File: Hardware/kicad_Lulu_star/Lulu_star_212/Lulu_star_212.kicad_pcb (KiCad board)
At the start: 2 copper layers, 16.7 x 14.9 mm, 8 parts, among them J1 Conn_01x03_Female, P1 Soldering_pad, Q1 Q_NMOS_GSD, T1 Q_NPN_BEC

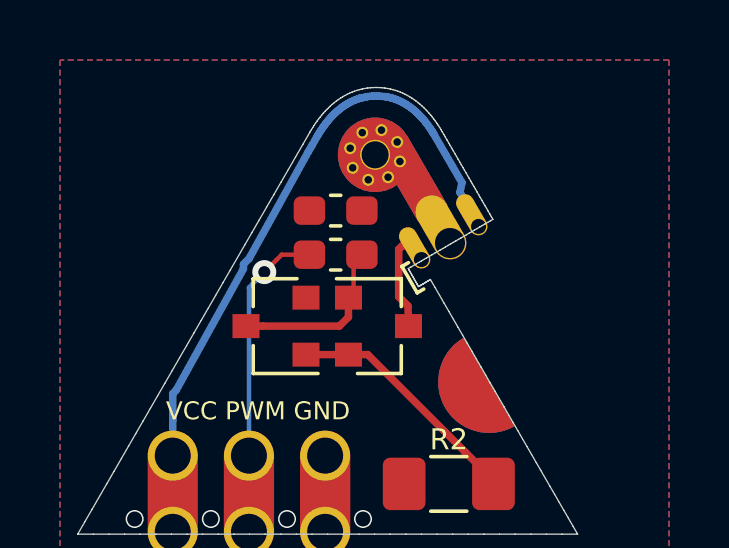
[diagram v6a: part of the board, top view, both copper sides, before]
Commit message: Correct the thermal pad GND connection
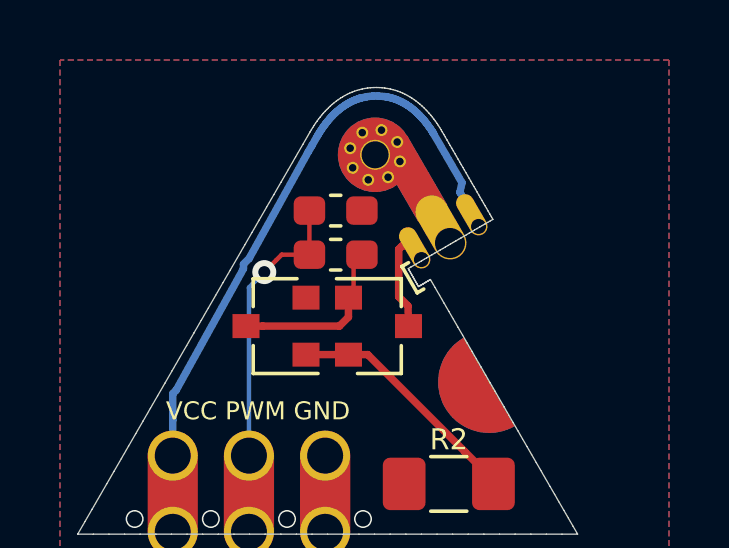
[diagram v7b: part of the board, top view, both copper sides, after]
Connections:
- LED1 pad : (no net) -> GND
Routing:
- net /PWM: track 7.80 -> 9.27 mm
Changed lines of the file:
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@@
     (thickness 1)
     (drawings 292)
-    (tracks 99)
+    (tracks 100)
     (zones 0)
     (modules 8)
@@
     (44 Edge.Cuts user)
     (45 Margin user)
-    (46 B.CrtYd user hide)
-    (47 F.CrtYd user hide)
-    (48 B.Fab user hide)
-    (49 F.Fab user hide)
+    (46 B.CrtYd user)
+    (47 F.CrtYd user)
+    (48 B.Fab user)
+    (49 F.Fab user)
   )
   (setup
@@
     (mod_text_size 1 1)
     (mod_text_width 0.15)
-    (pad_size 1.05 0.95)
+    (pad_size 2.48 2.48)
     (pad_drill 0)
     (pad_to_mask_clearance 0)
@@
     (add_net "Net-(Q1-Pad1)")
   )
-  (module Lulu_footprints:Lulu_side_LED locked (layer F.Cu)
+  (module Lulu_footprints:Lulu_side_LED (layer F.Cu)
     (at 74.64 35.4 30.1)
     (descr "LED Cree-XP http://www.cree.com/~/media/Files/Cree/LED-Components-and-Modules/XLamp/Data-and-Binning/XLampXPE2.pdf")
@@
       (effects (font (size 1 1) (thickness 0.15)))
     )
+    (fp_arc (start 0 0.6) (end -0.9 0.6) (angle -180) (layer F.Fab) (width 0.1))
+    (fp_line (start -1.778 -0.127) (end -1.524 -0.127) (layer F.SilkS) (width 0.12))
+    (fp_line (start -1.778 0.889) (end -1.778 -0.127) (layer F.SilkS) (width 0.12))
+    (fp_line (start -1.524 0.889) (end -1.778 0.889) (layer F.SilkS) (width 0.12))
+    (fp_line (start -1.523999 10.922) (end -1.524 -1.27) (layer F.CrtYd) (width 0.05))
+    (fp_line (start 1.524 10.922) (end -1.523999 10.922) (layer F.CrtYd) (width 0.05))
+    (fp_line (start 1.524 -1.27) (end 1.524 10.922) (layer F.CrtYd) (width 0.05))
+    (fp_line (start -1.524 -1.27) (end 1.524 -1.27) (layer F.CrtYd) (width 0.05))
+    (fp_poly (pts (xy -1.5 0) (xy 1.5 0) (xy 1.5 0.6) (xy -1.5 0.6)) (layer F.Fab) (width 0))
     (fp_poly (pts (xy -1.1 0.6) (xy 1.1 0.6) (xy 1.1 10.6) (xy -1.1 10.6)) (layer F.Fab) (width 0))
-    (fp_poly (pts (xy -1.5 0) (xy 1.5 0) (xy 1.5 0.6) (xy -1.5 0.6)) (layer F.Fab) (width 0))
-    (fp_line (start -1.524 -1.27) (end 1.524 -1.27) (layer F.CrtYd) (width 0.05))
-    (fp_line (start 1.524 -1.27) (end 1.524 10.922) (layer F.CrtYd) (width 0.05))
-    (fp_line (start 1.524 10.922) (end -1.523999 10.922) (layer F.CrtYd) (width 0.05))
-    (fp_line (start -1.523999 10.922) (end -1.524 -1.27) (layer F.CrtYd) (width 0.05))
-    (fp_line (start -1.524 0.889) (end -1.778 0.889) (layer F.SilkS) (width 0.12))
-    (fp_line (start -1.778 0.889) (end -1.778 -0.127) (layer F.SilkS) (width 0.12))
-    (fp_line (start -1.778 -0.127) (end -1.524 -0.127) (layer F.SilkS) (width 0.12))
-    (fp_arc (start 0 0.6) (end -0.9 0.6) (angle -180) (layer F.Fab) (width 0.1))
-    (pad "" smd custom (at -0.6858 -3.7973 30.1) (size 2.48 2.48) (layers B.Cu B.SilkS)
-      (zone_connect 2)
+    (pad 3 thru_hole circle (at -1.5494 -3.795372 30.1) (size 0.4 0.4) (drill 0.25) (layers *.Cu)
+      (net 2 GND))
+    (pad 3 thru_hole circle (at -0.685801 -3.795372 120.1) (size 1 1) (drill 0.9) (layers *.Cu)
+      (net 2 GND))
+    (pad 2 thru_hole oval (at 1.1 0 30.1) (size 0.6 1.5) (drill 0.5 (offset 0 -0.45)) (layers *.Cu *.Mask)
+      (net 6 +3V3) (zone_connect 0))
+    (pad 1 thru_hole oval (at -1.1 0 30.1) (size 0.6 1.5) (drill 0.5 (offset 0 -0.45)) (layers *.Cu *.Mask)
+      (net 5 "Net-(LED1-Pad1)") (zone_connect 0))
+    (pad 3 thru_hole oval (at 0 0 30.1) (size 1.1 2.3) (drill 1 (offset 0 -0.6)) (layers *.Cu *.Mask)
+      (net 2 GND) (zone_connect 2))
+    (pad 3 thru_hole circle (at 0.1651 -3.795372 30.1) (size 0.4 0.4) (drill 0.25) (layers *.Cu)
+      (net 2 GND))
+    (pad 3 thru_hole circle (at -0.6858 -2.9337 30.1) (size 0.4 0.4) (drill 0.25) (layers *.Cu)
+      (net 2 GND))
+    (pad 3 thru_hole circle (at -0.6858 -4.6482 30.1) (size 0.4 0.4) (drill 0.25) (layers *.Cu)
+      (net 2 GND))
+    (pad 3 thru_hole circle (at -0.08911 -4.400244 75.1) (size 0.4 0.4) (drill 0.25) (layers *.Cu)
+      (net 2 GND))
+    (pad 3 thru_hole circle (at -1.301444 -3.18791 75.1) (size 0.4 0.4) (drill 0.25) (layers *.Cu)
+      (net 2 GND))
+    (pad 3 thru_hole circle (at -0.081493 -3.189272 75.1) (size 0.4 0.4) (drill 0.25) (layers *.Cu)
+      (net 2 GND))
+    (pad 3 thru_hole circle (at -1.293827 -4.401606 75.1) (size 0.4 0.4) (drill 0.25) (layers *.Cu)
+      (net 2 GND))
+    (pad "" smd custom (at -0.685801 -3.795372 30.1) (size 2.48 2.48) (layers F.Cu F.Mask)
+      (net 2 GND) (zone_connect 2)
       (options (clearance outline) (anchor circle))
       (primitives
@@
            (xy 1.244601 2.652372) (xy 1.244601 -0.014628) (xy 0.127001 -0.014628) (xy 0.127001 2.652372)) (width 0))
       ))
-    (pad "" smd custom (at -0.685801 -3.795372 30.1) (size 2.48 2.48) (layers F.Cu F.Mask)
-      (zone_connect 2)
+    (pad "" smd custom (at -0.685801 -3.7973 30.1) (size 2.48 2.48) (layers B.Cu B.Mask)
+      (net 2 GND) (zone_connect 2)
       (options (clearance outline) (anchor circle))
       (primitives
@@
            (xy 1.244601 2.652372) (xy 1.244601 -0.014628) (xy 0.127001 -0.014628) (xy 0.127001 2.652372)) (width 0))
       ))
-    (pad 3 thru_hole circle (at -1.293827 -4.401606 75.1) (size 0.4 0.4) (drill 0.25) (layers *.Cu)
-      (net 2 GND))
-    (pad 3 thru_hole circle (at -0.081493 -3.189272 75.1) (size 0.4 0.4) (drill 0.25) (layers *.Cu)
-      (net 2 GND))
-    (pad 3 thru_hole circle (at -1.301444 -3.18791 75.1) (size 0.4 0.4) (drill 0.25) (layers *.Cu)
-      (net 2 GND))
-    (pad 3 thru_hole circle (at -0.08911 -4.400244 75.1) (size 0.4 0.4) (drill 0.25) (layers *.Cu)
-      (net 2 GND))
-    (pad 3 thru_hole circle (at -0.6858 -4.6482 30.1) (size 0.4 0.4) (drill 0.25) (layers *.Cu)
-      (net 2 GND))
-    (pad 3 thru_hole circle (at -0.6858 -2.9337 30.1) (size 0.4 0.4) (drill 0.25) (layers *.Cu)
-      (net 2 GND))
-    (pad 3 thru_hole circle (at 0.1651 -3.795372 30.1) (size 0.4 0.4) (drill 0.25) (layers *.Cu)
-      (net 2 GND))
-    (pad 3 thru_hole oval (at 0 0 30.1) (size 1.1 2.3) (drill 1 (offset 0 -0.6)) (layers *.Cu *.Mask)
-      (net 2 GND) (zone_connect 2))
-    (pad 1 thru_hole oval (at -1.1 0 30.1) (size 0.6 1.5) (drill 0.5 (offset 0 -0.45)) (layers *.Cu *.Mask)
-      (net 5 "Net-(LED1-Pad1)") (zone_connect 0))
-    (pad 2 thru_hole oval (at 1.1 0 30.1) (size 0.6 1.5) (drill 0.5 (offset 0 -0.45)) (layers *.Cu *.Mask)
-      (net 6 +3V3) (zone_connect 0))
-    (pad 3 thru_hole circle (at -0.685801 -3.795372 120.1) (size 1 1) (drill 0.9) (layers *.Cu)
-      (net 2 GND))
-    (pad 3 thru_hole circle (at -1.5494 -3.795372 30.1) (size 0.4 0.4) (drill 0.25) (layers *.Cu)
-      (net 2 GND))
     (model /home/chevrette/Bureau/Lulu/Hardware/kicad_Lulu_star/Lulu_star_212/packages3D/Lulu_LED_tube.wrl
       (at (xyz 0 0 0))
@@
   (segment (start 67.938 36.882) (end 68.050001 36.769999) (width 0.15) (layer B.Cu) (net 4))
   (segment (start 67.938 42.488) (end 67.938 36.882) (width 0.15) (layer B.Cu) (net 4))
+  (segment (start 69.955 34.32) (end 69.955 35.79) (width 0.15) (layer F.Cu) (net 4))
   (segment (start 72.93 35.61) (end 73.04 35.5) (width 0.25) (layer F.Cu) (net 5))
   (segment (start 72.93 37.19) (end 72.93 35.61) (width 0.25) (layer F.Cu) (net 5))
@@
     (connect_pads yes (clearance 0.15))
     (min_thickness 0.254)
-    (fill yes (arc_segments 32) (thermal_gap 0.508) (thermal_bridge_width 0.508))
+    (fill yes (arc_segments 32) (thermal_gap 0.508) (thermal_bridge_width 0.508) (smoothing fillet))
     (polygon
       (pts

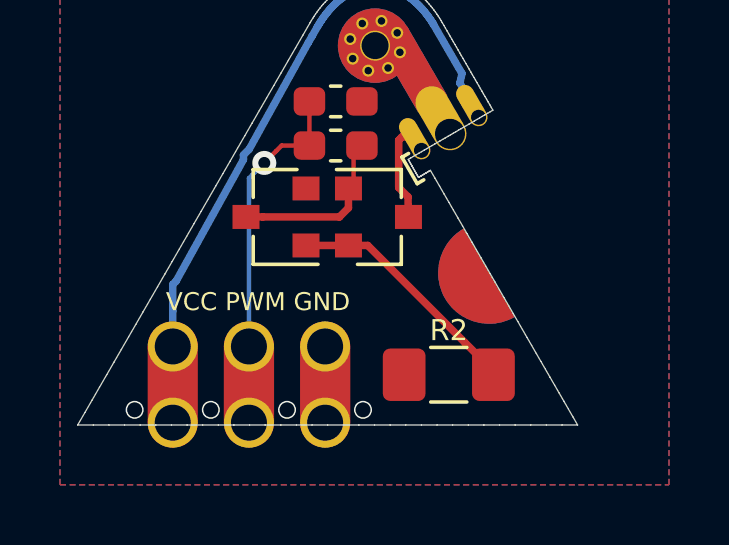
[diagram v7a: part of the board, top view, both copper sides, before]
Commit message: Updated ground plane
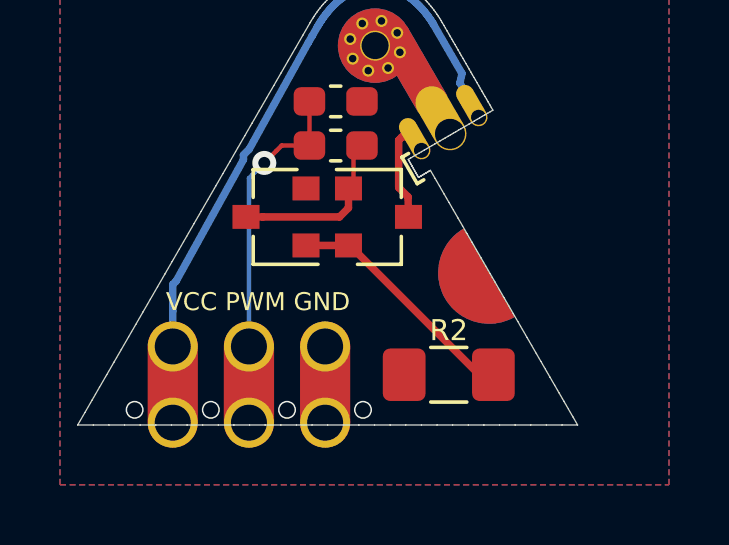
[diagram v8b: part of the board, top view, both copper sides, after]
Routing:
- net Net-(Q1-Pad2): track 8.76 -> 8.17 mm
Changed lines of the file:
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@@
   )
   (segment (start 69.7 39.12) (end 71.256 39.12) (width 0.25) (layer F.Cu) (net 1))
-  (segment (start 75.1295 42.35) (end 76.5375 43.758) (width 0.25) (layer F.Cu) (net 1))
-  (segment (start 71.256 39.12) (end 71.8995 39.12) (width 0.25) (layer F.Cu) (net 1))
-  (segment (start 71.8995 39.12) (end 75.1295 42.35) (width 0.25) (layer F.Cu) (net 1))
+  (segment (start 75.616 43.43) (end 76.0875 43.43) (width 0.25) (layer F.Cu) (net 1))
+  (segment (start 71.306 39.12) (end 75.616 43.43) (width 0.25) (layer F.Cu) (net 1))
+  (segment (start 71.256 39.12) (end 71.306 39.12) (width 0.25) (layer F.Cu) (net 1))
   (via (at 71.74 44.6) (size 0.6) (drill 0.5) (layers F.Cu B.Cu) (net 2))
   (via (at 69.208 44.6) (size 0.6) (drill 0.5) (layers F.Cu B.Cu) (net 2))
